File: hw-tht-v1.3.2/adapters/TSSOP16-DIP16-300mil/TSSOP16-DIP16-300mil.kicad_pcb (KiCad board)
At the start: 2 copper layers, 10.2 x 20.3 mm, 2 parts, among them J1 DIP-16 pins (8+8, 300 mil), U1 SN74CB3T3257

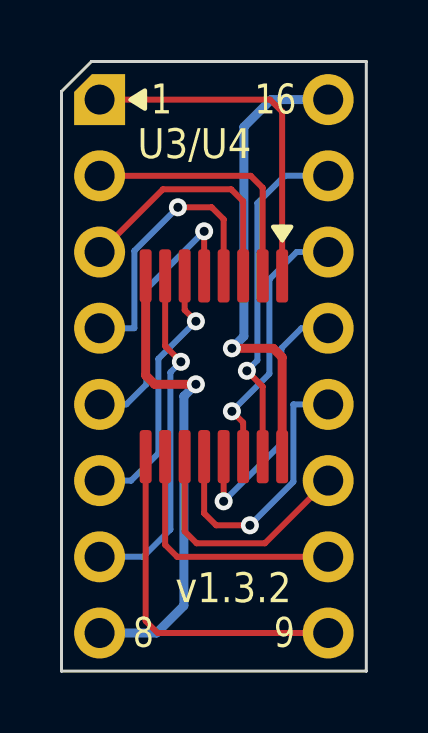
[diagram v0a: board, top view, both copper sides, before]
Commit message: THT v1.3.2 adapters: generic silkscreen
Drop the reference designators (U3/U4, U9) and the version number from
both adapter boards. The bottom now says what each board does, centred
on two lines (TSSOP-16 / DIP-16, TSSOP-20 / DIP-20), and still names the
chip it carries on PicoGUS. Copper unchanged; DRC with schematic parity
clean. Assembly views, DRC reports and the adapter STEP models (with
silkscreen) regenerated; README updated.

Co-Authored-By: Claude Opus 5.5 <noreply@anthropic.com>
Claude-Session: https://claude.ai/code/session_011utN3x8yYUNDvkpGCEq5yD
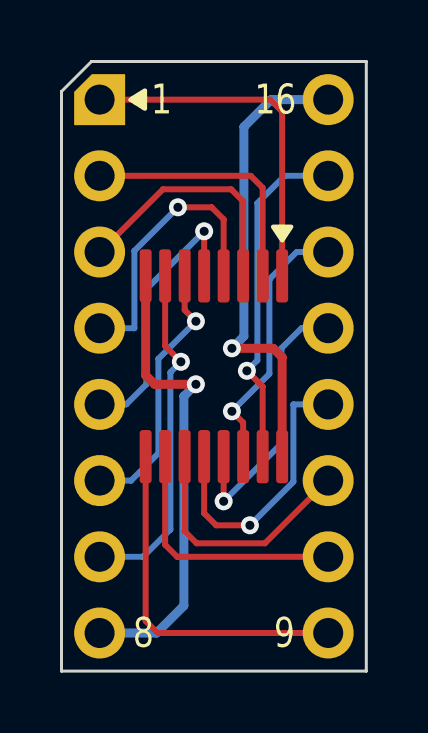
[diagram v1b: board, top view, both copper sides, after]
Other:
- board text added: "SN74CB3T3257"
- board text added: "TSSOP-16 DIP-16"
- board text removed: "PicoGUS v1.3.2 U3/U4"
- board text removed: "SN74CB3T3257 TSSOP16"
- board text removed: "U3/U4"
- board text removed: "v1.3.2"
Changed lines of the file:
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@@
 				(font
 					(size 1.27 1.27)
+					(thickness 0.15)
 				)
 			)
@@
 				(font
 					(size 1.27 1.27)
+					(thickness 0.15)
 				)
 			)
@@
 				(font
 					(size 1.27 1.27)
+					(thickness 0.15)
 				)
 			)
@@
 				(font
 					(size 1.27 1.27)
+					(thickness 0.15)
 				)
 			)
@@
 				(font
 					(size 1.27 1.27)
+					(thickness 0.15)
 				)
 			)
@@
 				(font
 					(size 1.27 1.27)
+					(thickness 0.15)
 				)
 			)
@@
 				(font
 					(size 1.27 1.27)
+					(thickness 0.15)
 				)
 			)
@@
 				(font
 					(size 1.27 1.27)
+					(thickness 0.15)
 				)
 			)
@@
 				(font
 					(size 1.27 1.27)
+					(thickness 0.15)
 				)
 			)
@@
 		)
 	)
-	(gr_text "U3/U4"
-		(at 103.16 101.49 0)
-		(layer "F.SilkS")
-		(effects
-			(font
-				(size 1 0.9)
-				(thickness 0.15)
-			)
-		)
-	)
-	(gr_text "v1.3.2"
-		(at 104.46 116.29 0)
-		(layer "F.SilkS")
-		(effects
-			(font
-				(size 1 0.9)
-				(thickness 0.15)
-			)
-		)
-	)
-	(gr_text "SN74CB3T3257  TSSOP16"
-		(at 101.76 108.89 90)
+	(gr_text "TSSOP-16\nDIP-16"
+		(at 103.81 112.18 0)
 		(layer "B.SilkS")
 		(effects
 			(font
-				(size 1 0.75)
+				(size 1 0.7)
 				(thickness 0.15)
 			)
@@
 		)
 	)
-	(gr_text "PicoGUS v1.3.2   U3/U4"
-		(at 105.86 108.89 90)
+	(gr_text "SN74CB3T3257"
+		(at 101.76 105.68 90)
 		(layer "B.SilkS")
 		(effects
